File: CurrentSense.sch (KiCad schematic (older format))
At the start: 7 parts, among them U5 INA139, U7 OPA340NA

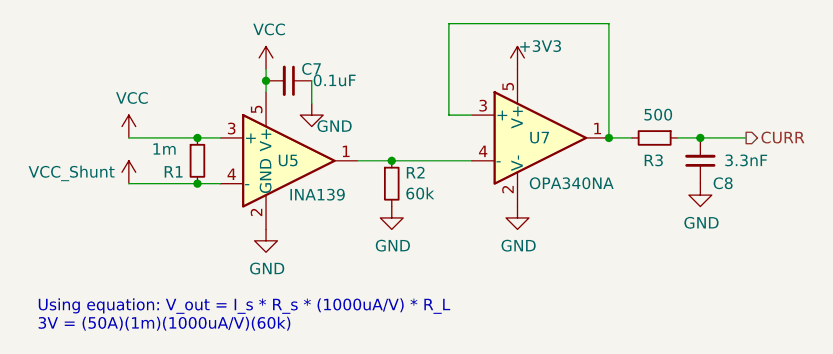
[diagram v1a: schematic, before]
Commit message: Addition of 5V Regulator
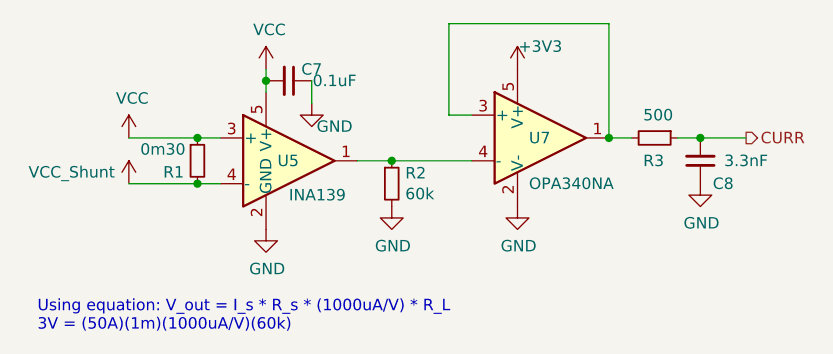
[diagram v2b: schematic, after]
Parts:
- R1: value 1m -> 0m30; footprint Footprints:SCMM2512S5-R001F -> Resistor_SMD:R_2512_6332Metric
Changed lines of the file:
@@
 P 4750 3800
 F 0 "R1" H 4600 3750 50  0000 L CNN
-F 1 "1m" H 4550 3850 50  0000 L CNN
-F 2 "Footprints:SCMM2512S5-R001F" H 4750 3800 50  0001 C CNN
+F 1 "0m30" H 4500 3850 50  0000 L CNN
+F 2 "Resistor_SMD:R_2512_6332Metric" H 4750 3800 50  0001 C CNN
 F 3 "~" H 4750 3800 50  0001 C CNN
 	1    4750 3800

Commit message: Added more PNGs
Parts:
- R1: value 0m30 -> 0m50
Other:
- note removed: "Using equation: V_out = I_s * R_s * (1000uA/V) * R_L\n3V = (50A)(1m)(1000uA/V)(60k)"
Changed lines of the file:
@@
 	1    0    0    -1
 $EndComp
-Text Notes 4050 4550 0    50   ~ 0
-Using equation: V_out = I_s * R_s * (1000uA/V) * R_L\n3V = (50A)(1m)(1000uA/V)(60k)
 Wire Wire Line
 	5950 3800 5600 3800
@@
 P 4750 3800
 F 0 "R1" H 4600 3750 50  0000 L CNN
-F 1 "0m30" H 4500 3850 50  0000 L CNN
+F 1 "0m50" H 4500 3850 50  0000 L CNN
 F 2 "Resistor_SMD:R_2512_6332Metric" H 4750 3800 50  0001 C CNN
 F 3 "~" H 4750 3800 50  0001 C CNN

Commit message: Some graphical additions
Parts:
- R1: footprint Resistor_SMD:R_2512_6332Metric -> Resistor_SMD:R_Shunt_Vishay_WSLP2726
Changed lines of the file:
@@
 F 0 "R1" H 4600 3750 50  0000 L CNN
 F 1 "0m50" H 4500 3850 50  0000 L CNN
-F 2 "Resistor_SMD:R_2512_6332Metric" H 4750 3800 50  0001 C CNN
+F 2 "Resistor_SMD:R_Shunt_Vishay_WSLP2726" H 4750 3800 50  0001 C CNN
 F 3 "~" H 4750 3800 50  0001 C CNN
 	1    4750 3800

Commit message: Updated PNGS
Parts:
- R1: value 0m50 -> 0m30
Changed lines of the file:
@@
 P 4750 3800
 F 0 "R1" H 4600 3750 50  0000 L CNN
-F 1 "0m50" H 4500 3850 50  0000 L CNN
+F 1 "0m30" H 4500 3850 50  0000 L CNN
 F 2 "Resistor_SMD:R_Shunt_Vishay_WSLP2726" H 4750 3800 50  0001 C CNN
 F 3 "~" H 4750 3800 50  0001 C CNN
